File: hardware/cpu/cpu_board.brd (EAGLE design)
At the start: 167.9 x 122.5 mm, 53 parts, among them IC4 7404N, IC5 7400N, IC6 74HCT139N, IC7 7400N, IC9 74HCT138N, X1 22-23-2041

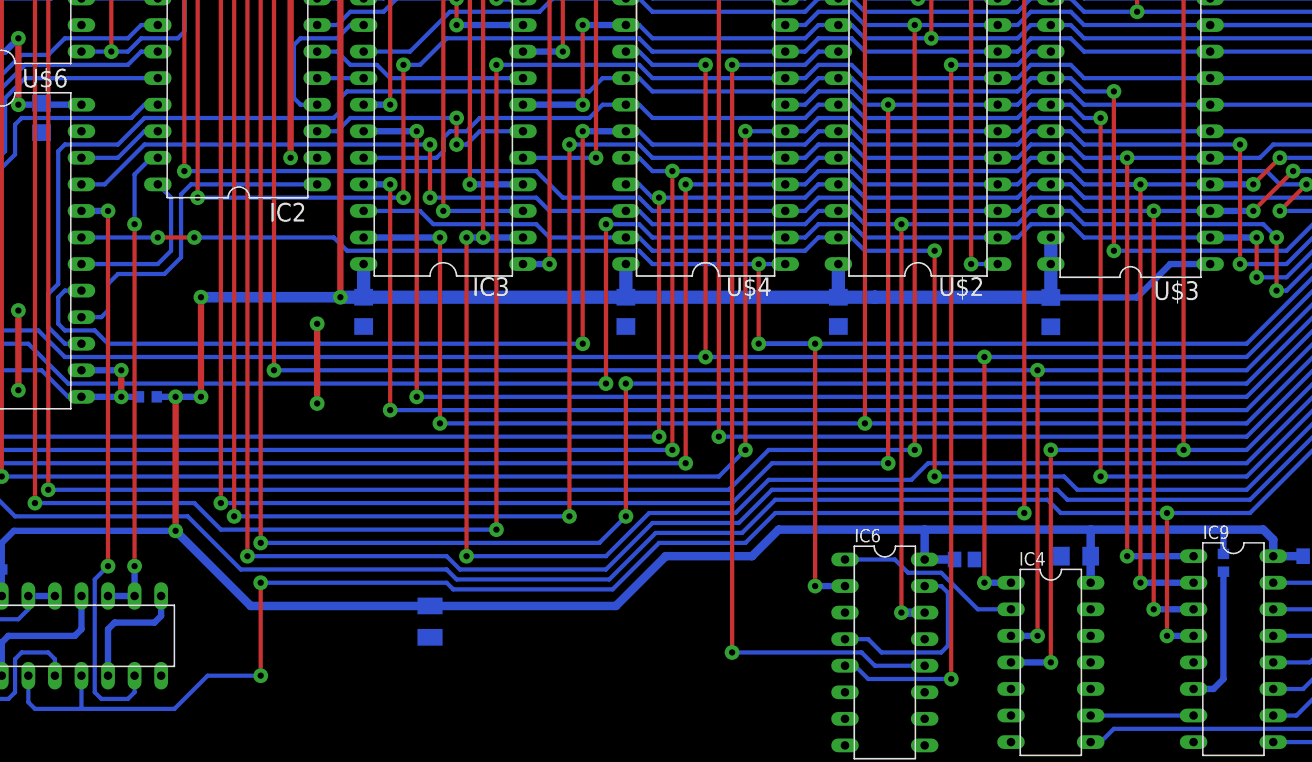
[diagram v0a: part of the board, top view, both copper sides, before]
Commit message: Bug in memory address decoder fixed
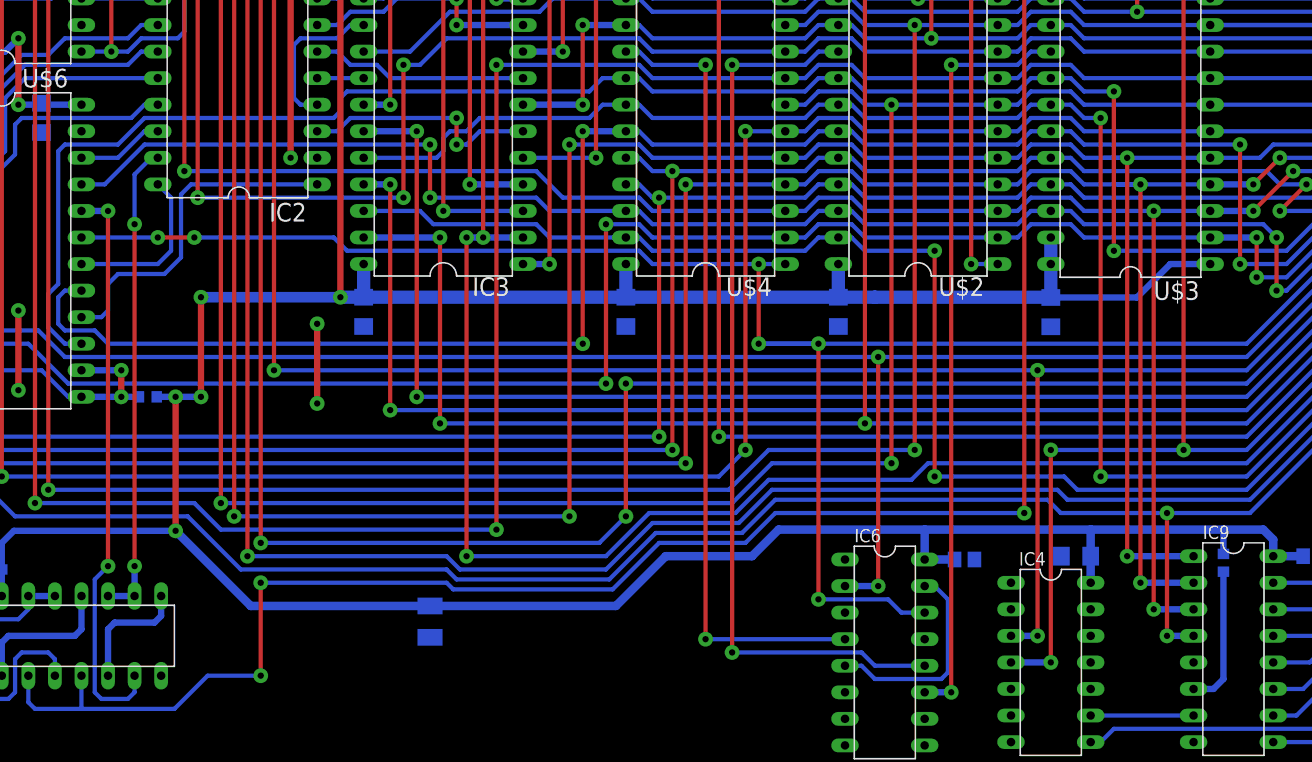
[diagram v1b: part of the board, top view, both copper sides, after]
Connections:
- removed net !A15: IC4.2, IC6.1
- new net CS_RAM: IC6.4, U$4.20
- net A13: no longer IC6.14
- net A14: now also IC6.14; no longer IC6.2
- net A15: now also IC6.2; no longer IC4.1, U$4.20
- net CS_EPROM: now also IC6.11; no longer IC6.5
- net GND: now also IC4.1, IC6.1
- net N$19: now also IC6.5; no longer IC6.4
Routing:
- net CS_RAM: track 0.00 -> 76.4 mm, vias 0 -> 2
- net A13: track 192.7 -> 153.3 mm, vias 6 -> 4
- net A15: track 223.5 -> 188.3 mm, vias 4 -> 2
- net !A15: track 17.8 -> 0.00 mm
- net A14: track 179.0 -> 188.4 mm
- net CS_EPROM: track 79.5 -> 72.6 mm
- net N$19: track 18.2 -> 20.4 mm

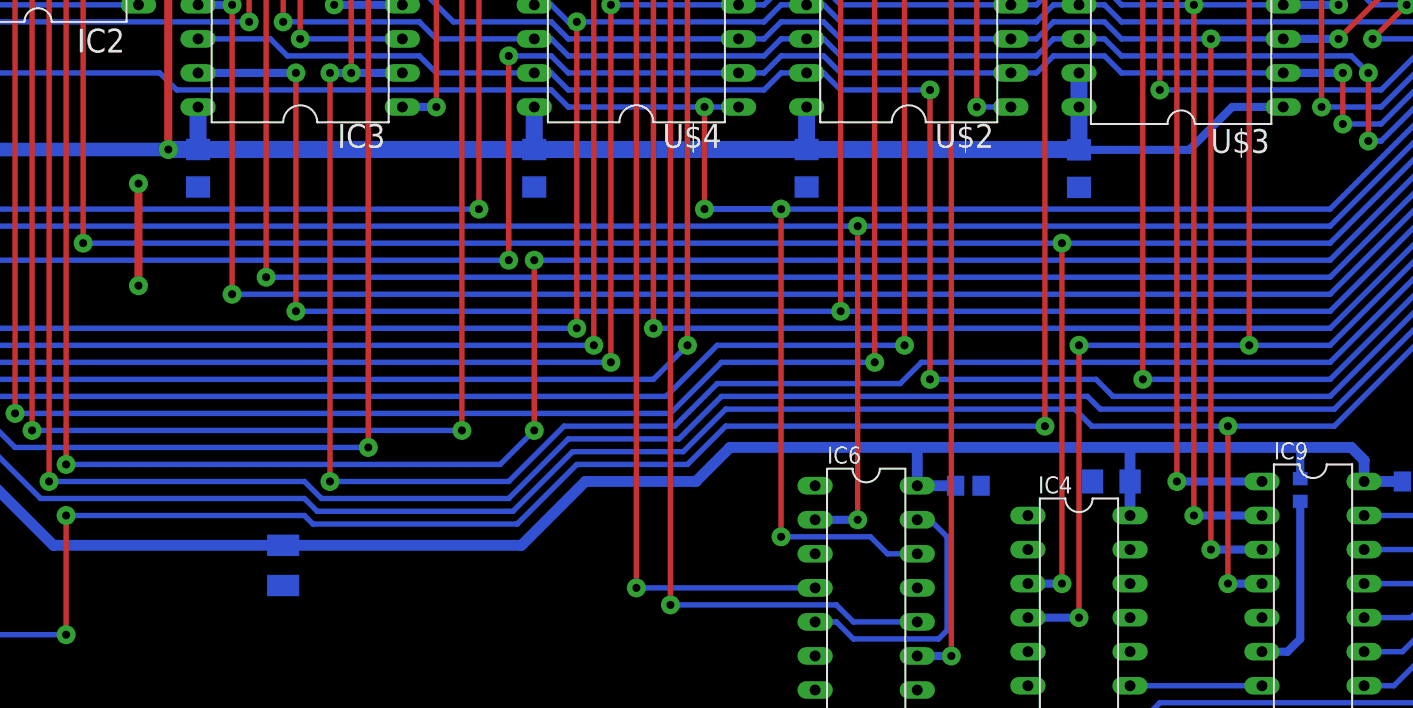
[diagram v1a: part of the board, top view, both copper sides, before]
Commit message: AEN signal connected to memory address decoder
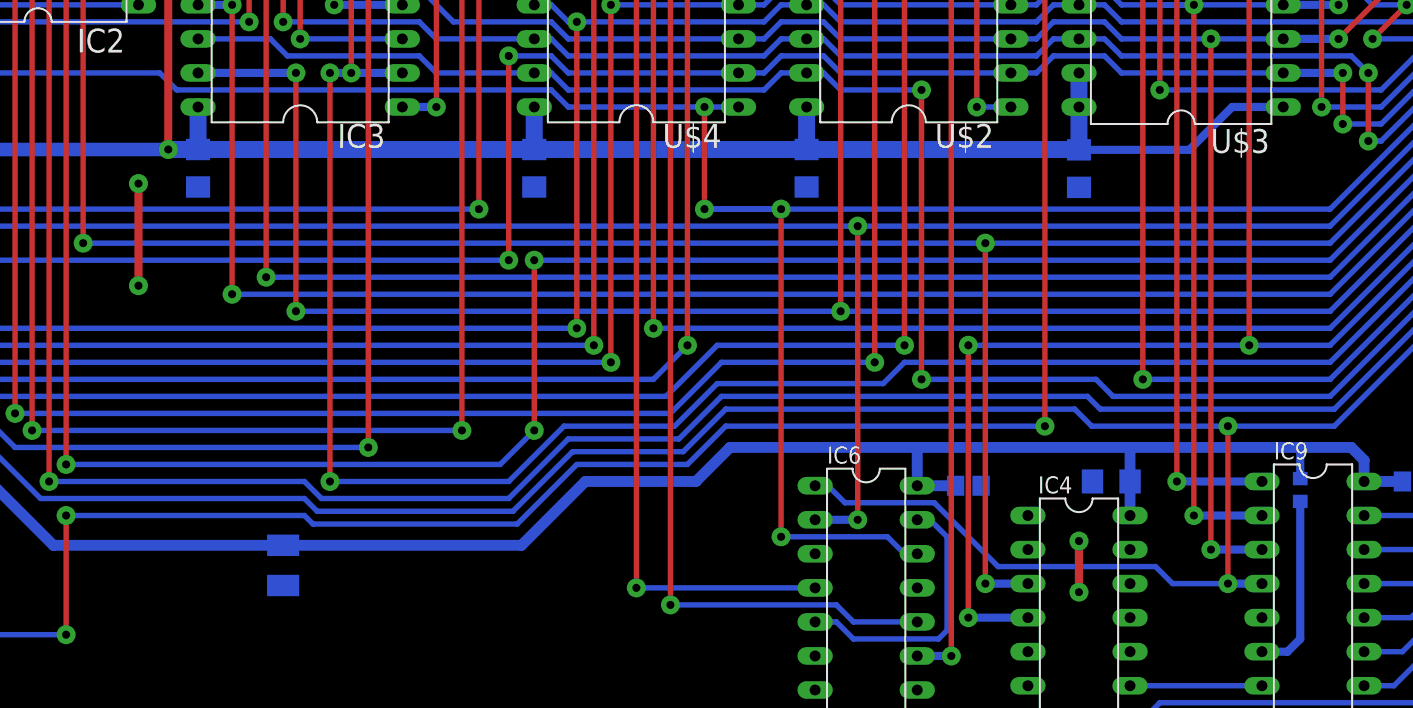
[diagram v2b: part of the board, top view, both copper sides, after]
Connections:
- net AEN: now also IC6.1
- net GND: no longer IC6.1
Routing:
- net AEN: track 306.4 -> 340.2 mm
- net !RESET: track 144.2 -> 153.1 mm
- net GND: track 115.1 -> 118.9 mm, vias 16 -> 18
- net RESET: track 238.0 -> 238.7 mm
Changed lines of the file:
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@@
 <contactref element="IC7" pad="1"/>
 <contactref element="C15" pad="2"/>
-<contactref element="IC6" pad="1"/>
 <contactref element="IC4" pad="1"/>
+<via x="118.745" y="15.24" extent="1-16" drill="0.6" diameter="1.4224" shape="octagon"/>
+<via x="118.745" y="19.05" extent="1-16" drill="0.6" diameter="1.4224" shape="octagon"/>
+<wire x1="118.745" y1="15.24" x2="118.745" y2="19.05" width="0.6096" layer="1"/>
 </signal>
 <signal name="D0">
@@
 <wire x1="98.425" y1="53.975" x2="99.695" y2="53.975" width="0.4064" layer="16"/>
 <wire x1="99.695" y1="53.975" x2="100.965" y2="52.705" width="0.4064" layer="16"/>
-<wire x1="100.965" y1="52.705" x2="107.6325" y2="52.705" width="0.4064" layer="16"/>
-<via x="107.6325" y="52.705" extent="1-16" drill="0.6" diameter="1.4224" shape="octagon"/>
-<wire x1="107.6325" y1="52.705" x2="107.6325" y2="31.115" width="0.4064" layer="1"/>
-<via x="107.6325" y="31.115" extent="1-16" drill="0.6" diameter="1.4224" shape="octagon"/>
-<wire x1="107.6325" y1="31.115" x2="120.015" y2="31.115" width="0.4064" layer="16"/>
+<wire x1="100.965" y1="52.705" x2="106.9975" y2="52.705" width="0.4064" layer="16"/>
+<via x="106.9975" y="52.705" extent="1-16" drill="0.6" diameter="1.4224" shape="octagon"/>
+<wire x1="106.9975" y1="52.705" x2="106.9975" y2="31.115" width="0.4064" layer="1"/>
+<via x="106.9975" y="31.115" extent="1-16" drill="0.6" diameter="1.4224" shape="octagon"/>
 <wire x1="120.015" y1="31.115" x2="121.285" y2="29.845" width="0.4064" layer="16"/>
 <wire x1="121.285" y1="29.845" x2="137.4775" y2="29.845" width="0.4064" layer="16"/>
@@
 <wire x1="158.115" y1="47.625" x2="156.845" y2="46.355" width="0.4064" layer="16"/>
 <wire x1="156.845" y1="46.355" x2="153.9875" y2="46.355" width="0.4064" layer="16"/>
+<wire x1="106.9975" y1="31.115" x2="120.015" y2="31.115" width="0.4064" layer="16"/>
 </signal>
 <signal name="IO_WR">
@@
 <contactref element="SV2" pad="29"/>
 <contactref element="IC6" pad="14"/>
-<wire x1="96.52" y1="19.3675" x2="103.1875" y2="19.3675" width="0.4064" layer="16"/>
-<wire x1="103.1875" y1="19.3675" x2="104.4575" y2="18.0975" width="0.4064" layer="16"/>
-<wire x1="104.4575" y1="18.0975" x2="106.68" y2="18.0975" width="0.4064" layer="16"/>
+<wire x1="96.52" y1="19.3675" x2="104.4575" y2="19.3675" width="0.4064" layer="16"/>
+<wire x1="104.4575" y1="19.3675" x2="105.7275" y2="18.0975" width="0.4064" layer="16"/>
+<wire x1="105.7275" y1="18.0975" x2="106.68" y2="18.0975" width="0.4064" layer="16"/>
 </signal>
 <signal name="BANK_A14">
@@
 <wire x1="80.3275" y1="27.6225" x2="88.5825" y2="27.6225" width="0.4064" layer="16"/>
 <wire x1="88.5825" y1="27.6225" x2="91.7575" y2="30.7975" width="0.4064" layer="16"/>
-<wire x1="91.7575" y1="30.7975" x2="105.41" y2="30.7975" width="0.4064" layer="16"/>
-<wire x1="105.41" y1="30.7975" x2="106.9975" y2="32.385" width="0.4064" layer="16"/>
-<wire x1="106.9975" y1="32.385" x2="137.4775" y2="32.385" width="0.4064" layer="16"/>
+<wire x1="91.7575" y1="30.7975" x2="104.14" y2="30.7975" width="0.4064" layer="16"/>
 <contactref element="SV2" pad="38"/>
 <wire x1="137.4775" y1="32.385" x2="153.9875" y2="48.895" width="0.4064" layer="16"/>
 <wire x1="158.115" y1="50.165" x2="156.845" y2="48.895" width="0.4064" layer="16"/>
 <wire x1="156.845" y1="48.895" x2="153.9875" y2="48.895" width="0.4064" layer="16"/>
+<wire x1="137.4775" y1="32.385" x2="105.7275" y2="32.385" width="0.4064" layer="16"/>
+<wire x1="105.7275" y1="32.385" x2="104.14" y2="30.7975" width="0.4064" layer="16"/>
 </signal>
 <signal name="N$5">
@@
 <wire x1="51.1175" y1="87.9475" x2="50.165" y2="86.995" width="0.4064" layer="16"/>
 <wire x1="44.45" y1="86.995" x2="48.5775" y2="86.995" width="0.6096" layer="16"/>
-<via x="117.475" y="15.875" extent="1-16" drill="0.6" diameter="1.4224" shape="octagon"/>
-<wire x1="117.475" y1="15.875" x2="117.475" y2="41.275" width="0.4064" layer="1"/>
-<via x="117.475" y="41.275" extent="1-16" drill="0.6" diameter="1.4224" shape="octagon"/>
-<wire x1="137.4775" y1="41.275" x2="117.475" y2="41.275" width="0.4064" layer="16"/>
-<wire x1="117.475" y1="41.275" x2="44.45" y2="41.275" width="0.4064" layer="16"/>
+<via x="111.76" y="15.875" extent="1-16" drill="0.6" diameter="1.4224" shape="octagon"/>
+<wire x1="111.76" y1="15.875" x2="111.76" y2="41.275" width="0.4064" layer="1"/>
+<via x="111.76" y="41.275" extent="1-16" drill="0.6" diameter="1.4224" shape="octagon"/>
+<wire x1="137.4775" y1="41.275" x2="111.76" y2="41.275" width="0.4064" layer="16"/>
+<wire x1="111.76" y1="41.275" x2="44.45" y2="41.275" width="0.4064" layer="16"/>
 <wire x1="51.1175" y1="87.9475" x2="85.4075" y2="87.9475" width="0.4064" layer="16"/>
 <contactref element="SV2" pad="31"/>
 <contactref element="IC4" pad="3"/>
-<wire x1="114.935" y1="15.875" x2="117.475" y2="15.875" width="0.6096" layer="16"/>
+<wire x1="114.935" y1="15.875" x2="111.76" y2="15.875" width="0.6096" layer="16"/>
 </signal>
 <signal name="FI1">
@@
 <wire x1="156.845" y1="43.815" x2="158.115" y2="45.085" width="0.4064" layer="16"/>
 <wire x1="36.195" y1="27.305" x2="41.275" y2="22.225" width="0.4064" layer="16"/>
+<contactref element="IC6" pad="1"/>
+<wire x1="99.06" y1="23.1775" x2="100.0125" y2="23.1775" width="0.4064" layer="16"/>
+<wire x1="100.0125" y1="23.1775" x2="101.2825" y2="21.9075" width="0.4064" layer="16"/>
+<wire x1="101.2825" y1="21.9075" x2="107.95" y2="21.9075" width="0.4064" layer="16"/>
+<wire x1="107.95" y1="21.9075" x2="112.7125" y2="17.145" width="0.4064" layer="16"/>
+<wire x1="112.7125" y1="17.145" x2="124.46" y2="17.145" width="0.4064" layer="16"/>
+<wire x1="124.46" y1="17.145" x2="125.73" y2="15.875" width="0.4064" layer="16"/>
+<wire x1="125.73" y1="15.875" x2="129.8575" y2="15.875" width="0.4064" layer="16"/>
 </signal>
 <signal name="START_MEM_SWITCH">
@@
 <signal name="!RESET">
 <contactref element="U$1" pad="14"/>
-<via x="118.745" y="13.335" extent="1-16" drill="0.6" diameter="1.4224" shape="octagon"/>
-<wire x1="118.745" y1="13.335" x2="118.745" y2="33.655" width="0.4064" layer="1"/>
-<via x="118.745" y="33.655" extent="1-16" drill="0.6" diameter="1.4224" shape="octagon"/>
-<wire x1="118.745" y1="33.655" x2="131.445" y2="33.655" width="0.4064" layer="16"/>
+<via x="110.49" y="13.335" extent="1-16" drill="0.6" diameter="1.4224" shape="octagon"/>
+<wire x1="110.49" y1="13.335" x2="110.49" y2="33.655" width="0.4064" layer="1"/>
+<via x="110.49" y="33.655" extent="1-16" drill="0.6" diameter="1.4224" shape="octagon"/>
+<wire x1="110.49" y1="33.655" x2="131.445" y2="33.655" width="0.4064" layer="16"/>
 <via x="131.445" y="33.655" extent="1-16" drill="0.6" diameter="1.4224" shape="octagon"/>
 <wire x1="131.445" y1="33.655" x2="131.445" y2="99.3775" width="0.4064" layer="1"/>
@@
 <contactref element="SV2" pad="37"/>
 <contactref element="IC4" pad="4"/>
-<wire x1="114.935" y1="13.335" x2="118.745" y2="13.335" width="0.6096" layer="16"/>
+<wire x1="114.935" y1="13.335" x2="110.49" y2="13.335" width="0.6096" layer="16"/>
 <wire x1="126.365" y1="104.4575" x2="131.445" y2="99.3775" width="0.4064" layer="16"/>
 </signal>

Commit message: PCB optimized
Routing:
- net AEN: track 340.2 -> 315.3 mm, vias 8 -> 10
- net GND: track 118.9 -> 115.1 mm, vias 18 -> 16
- net VCC: track 627.6 -> 624.8 mm

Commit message: AEN removed from memory address decoder
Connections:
- net AEN: no longer IC6.1
- net GND: now also IC6.1
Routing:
- net AEN: track 315.3 -> 309.9 mm
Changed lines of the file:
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@@
 <contactref element="C15" pad="2"/>
 <contactref element="IC4" pad="1"/>
+<contactref element="IC6" pad="1"/>
 </signal>
 <signal name="D0">
@@
 <wire x1="156.845" y1="43.815" x2="158.115" y2="45.085" width="0.4064" layer="16"/>
 <wire x1="36.195" y1="27.305" x2="43.18" y2="20.32" width="0.4064" layer="16"/>
-<contactref element="IC6" pad="1"/>
-<wire x1="99.06" y1="23.1775" x2="100.0125" y2="23.1775" width="0.4064" layer="16"/>
 <wire x1="43.18" y1="20.32" x2="76.835" y2="20.32" width="0.4064" layer="16"/>
 <wire x1="76.835" y1="20.32" x2="81.28" y2="24.765" width="0.4064" layer="16"/>
 <wire x1="81.28" y1="24.765" x2="89.535" y2="24.765" width="0.4064" layer="16"/>
 <wire x1="92.075" y1="27.305" x2="89.535" y2="24.765" width="0.4064" layer="16"/>
-<wire x1="99.06" y1="23.1775" x2="103.505" y2="23.1775" width="0.4064" layer="16"/>
 <via x="103.505" y="23.1775" extent="1-16" drill="0.6" diameter="1.4224" shape="octagon"/>
 <wire x1="103.505" y1="23.1775" x2="103.505" y2="27.305" width="0.4064" layer="1"/>
